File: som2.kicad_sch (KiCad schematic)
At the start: 4 parts

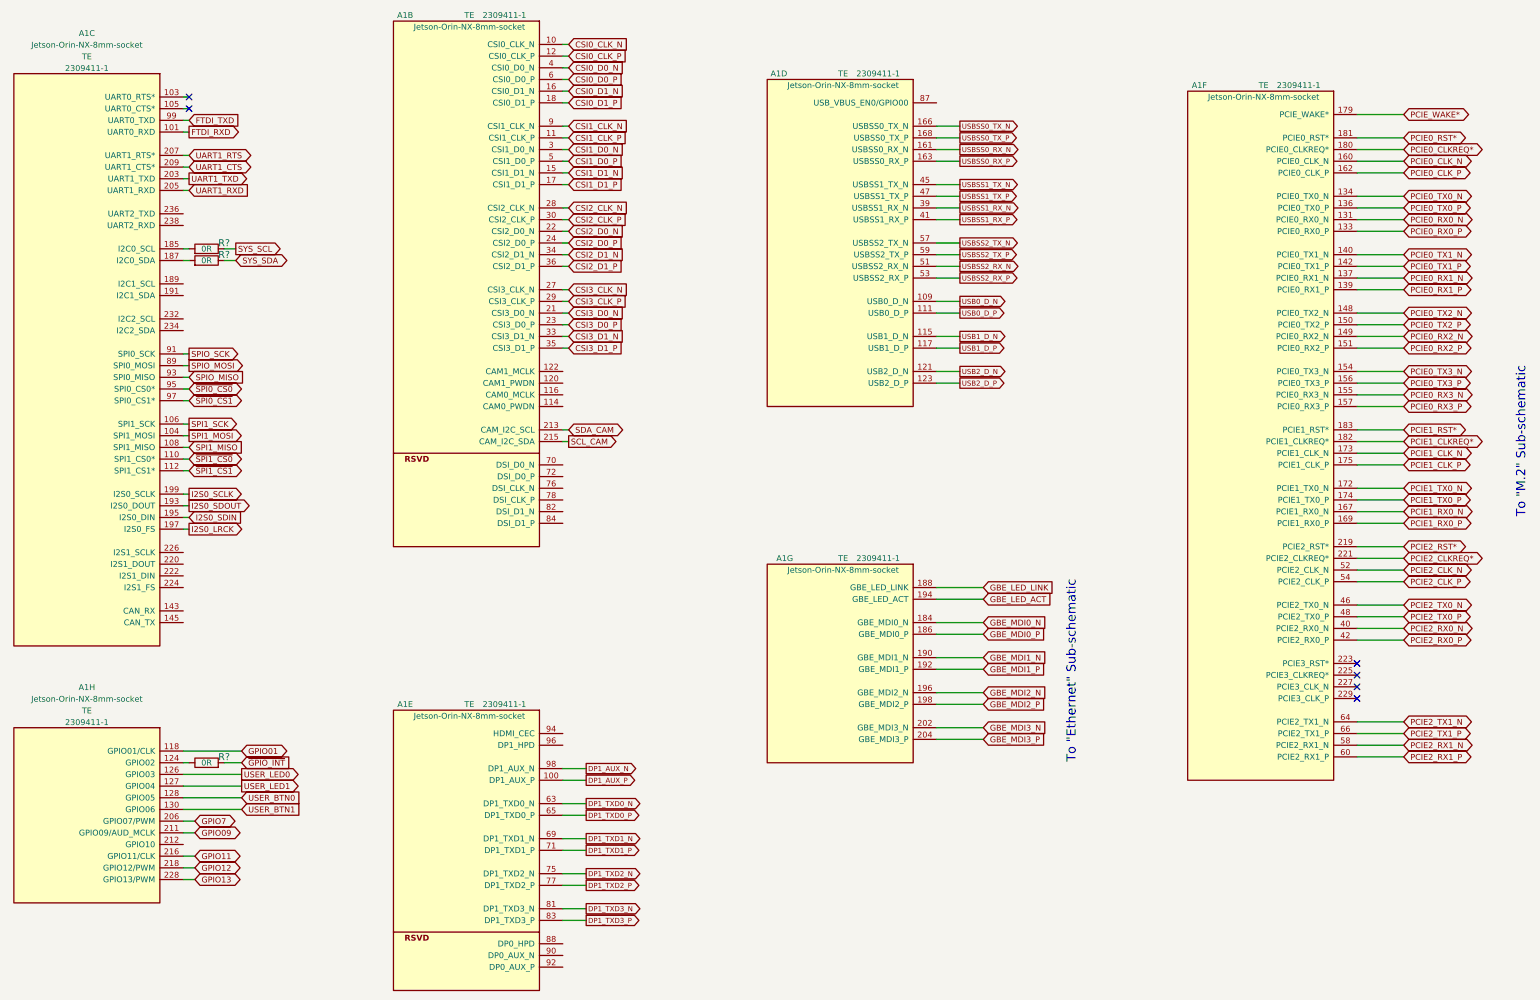
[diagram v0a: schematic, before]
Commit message: Cleaned up schematics, added debug connector, user LEDs and buttons. Connected misc. signals
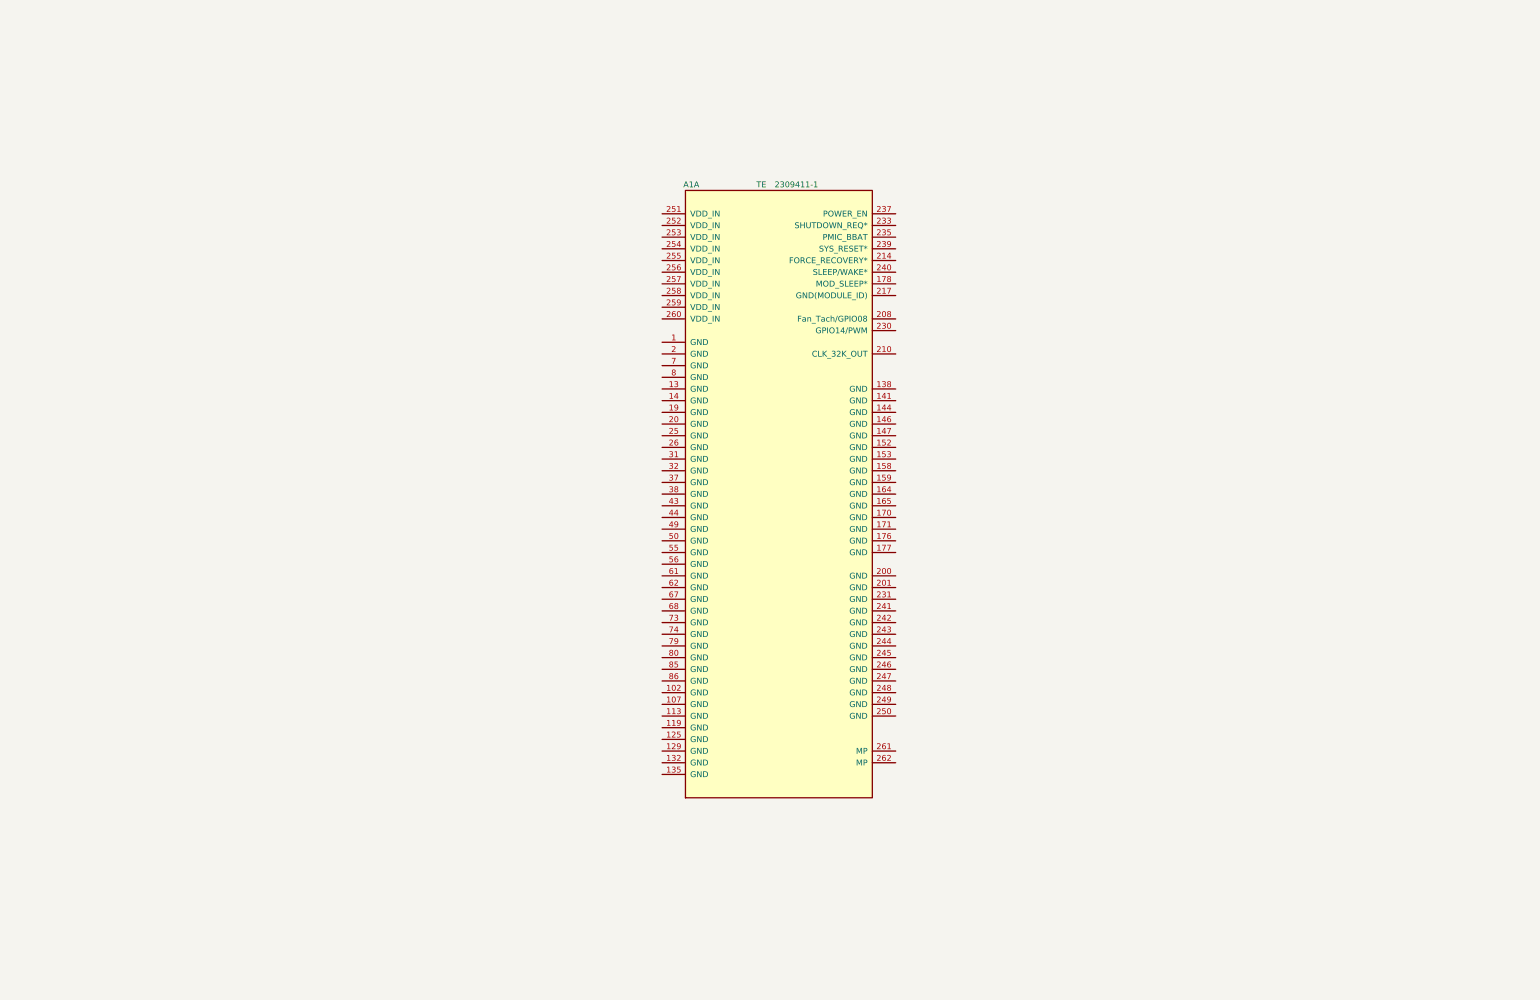
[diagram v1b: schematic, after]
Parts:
- removed A1: Jetson-Orin-NX-8mm-socket, antmicro-footprints:2309411-1, symbol antmicroSoMConnectors:Jetson-Orin-NX-8mm-socket
- removed R? (x2): ~, symbol antmicroResistors0402:R_0R_0402
- removed R?: R_0R_0402, antmicro-footprints:0402-res, symbol antmicroResistors0402:R_0R_0402
- added A1: (no value), symbol antmicroSoMConnectors:Jetson-Orin-NX-8mm-socket
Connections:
- no-connect marks 6 -> 0
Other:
- note removed: "To "Ethernet" Sub-schematic"
- note removed: "To "M.2" Sub-schematic"
